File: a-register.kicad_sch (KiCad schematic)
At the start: 12 parts

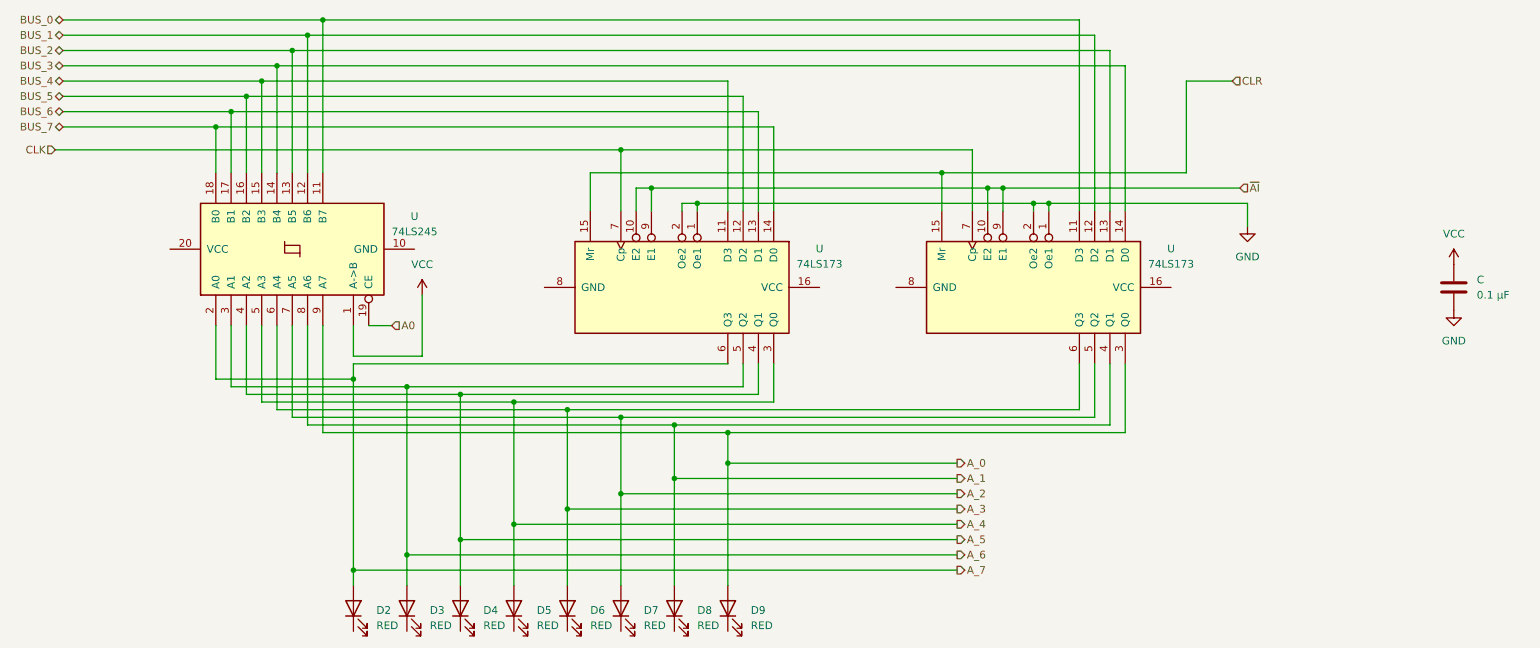
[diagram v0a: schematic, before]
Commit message: Added the ALU and flags register schematic.
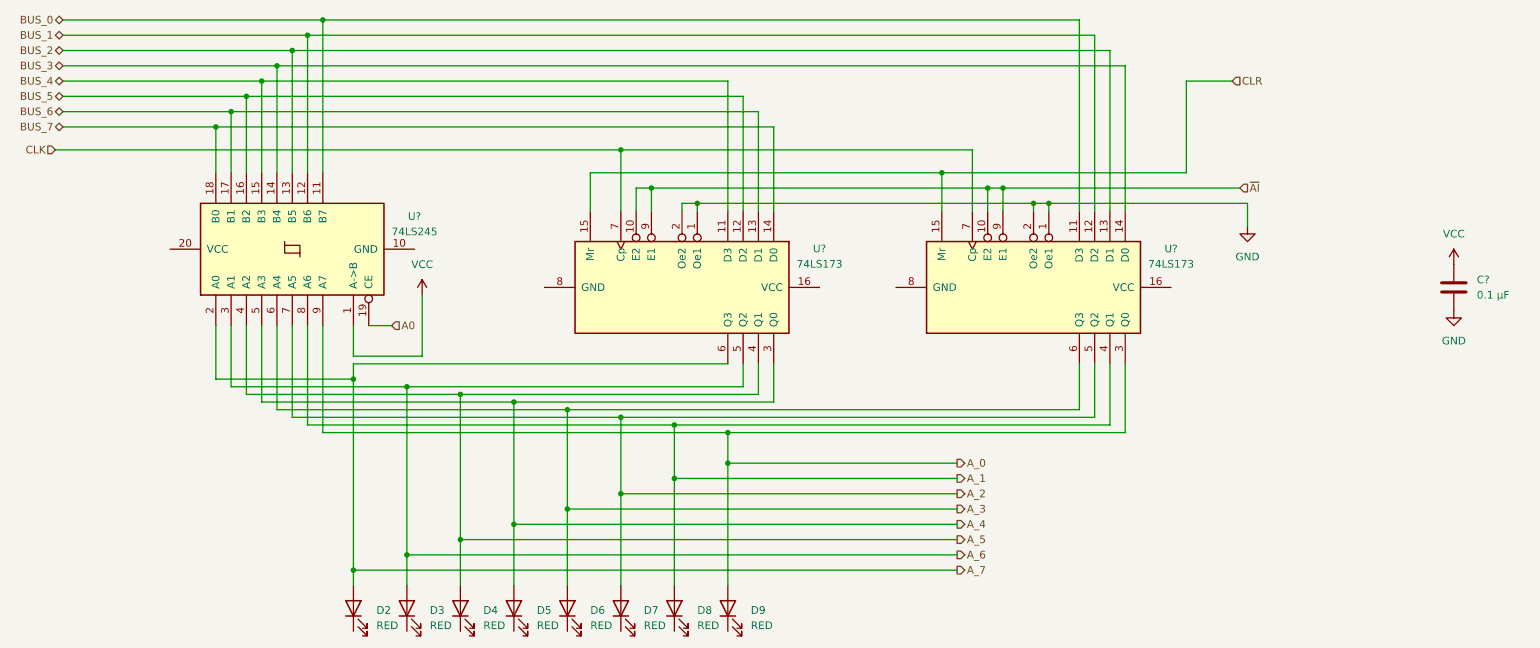
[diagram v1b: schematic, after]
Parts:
- renumbered C to C?, U to U?
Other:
- title: (none) -> 8 bit PC
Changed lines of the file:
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@@
 	(generator_version "9.0")
 	(paper "A4")
+	(title_block
+		(title "8 bit PC")
+		(date "2025-10-14")
+		(rev "1")
+	)
 	(junction
 		(at 57.15 35.56)
@@
 		(instances
 			(project "8-Bit-PC"
-				(path "/48633dea-2de9-4b6f-aeff-2ee54233f918/01639e59-f640-4704-bff8-92b5a7e3f002"
-					(reference "D16")
-					(unit 1)
-				)
 				(path "/48633dea-2de9-4b6f-aeff-2ee54233f918/0da64945-ad09-4cb6-87e6-9538c18b83c8"
 					(reference "D8")
@@
 		(instances
 			(project "8-Bit-PC"
-				(path "/48633dea-2de9-4b6f-aeff-2ee54233f918/01639e59-f640-4704-bff8-92b5a7e3f002"
-					(reference "D15")
-					(unit 1)
-				)
 				(path "/48633dea-2de9-4b6f-aeff-2ee54233f918/0da64945-ad09-4cb6-87e6-9538c18b83c8"
 					(reference "D7")
@@
 		(dnp no)
 		(fields_autoplaced yes)
-		(property "Reference" "U"
+		(property "Reference" "U?"
 			(at 213.36 58.3498 90)
 			(effects
@@
 		(instances
 			(project "8-Bit-PC"
-				(path "/48633dea-2de9-4b6f-aeff-2ee54233f918/01639e59-f640-4704-bff8-92b5a7e3f002"
-					(reference "U12")
+				(path "/48633dea-2de9-4b6f-aeff-2ee54233f918/0da64945-ad09-4cb6-87e6-9538c18b83c8"
+					(reference "U?")
 					(unit 1)
 				)
@@
 		(dnp no)
 		(fields_autoplaced yes)
-		(property "Reference" "#PWR"
+		(property "Reference" "#PWR?"
 			(at 260.35 74.93 0)
 			(effects
@@
 		(instances
 			(project "8-Bit-PC"
-				(path "/48633dea-2de9-4b6f-aeff-2ee54233f918/01639e59-f640-4704-bff8-92b5a7e3f002"
-					(reference "#PWR017")
+				(path "/48633dea-2de9-4b6f-aeff-2ee54233f918/0da64945-ad09-4cb6-87e6-9538c18b83c8"
+					(reference "#PWR?")
 					(unit 1)
 				)
@@
 		(dnp no)
 		(fields_autoplaced yes)
-		(property "Reference" "U"
+		(property "Reference" "U?"
 			(at 87.63 52.9746 90)
 			(effects
@@
 		(instances
 			(project "8-Bit-PC"
-				(path "/48633dea-2de9-4b6f-aeff-2ee54233f918/01639e59-f640-4704-bff8-92b5a7e3f002"
-					(reference "U10")
+				(path "/48633dea-2de9-4b6f-aeff-2ee54233f918/0da64945-ad09-4cb6-87e6-9538c18b83c8"
+					(reference "U?")
 					(unit 1)
 				)
@@
 		(dnp no)
 		(fields_autoplaced yes)
-		(property "Reference" "#PWR"
+		(property "Reference" "#PWR?"
 			(at 226.06 60.96 0)
 			(effects
@@
 		(instances
 			(project "8-Bit-PC"
-				(path "/48633dea-2de9-4b6f-aeff-2ee54233f918/01639e59-f640-4704-bff8-92b5a7e3f002"
-					(reference "#PWR015")
+				(path "/48633dea-2de9-4b6f-aeff-2ee54233f918/0da64945-ad09-4cb6-87e6-9538c18b83c8"
+					(reference "#PWR?")
 					(unit 1)
 				)
@@
 		(dnp no)
 		(fields_autoplaced yes)
-		(property "Reference" "#PWR"
+		(property "Reference" "#PWR?"
 			(at 260.35 64.77 0)
 			(effects
@@
 		(instances
 			(project "8-Bit-PC"
-				(path "/48633dea-2de9-4b6f-aeff-2ee54233f918/01639e59-f640-4704-bff8-92b5a7e3f002"
-					(reference "#PWR016")
+				(path "/48633dea-2de9-4b6f-aeff-2ee54233f918/0da64945-ad09-4cb6-87e6-9538c18b83c8"
+					(reference "#PWR?")
 					(unit 1)
 				)
@@
 		(instances
 			(project "8-Bit-PC"
-				(path "/48633dea-2de9-4b6f-aeff-2ee54233f918/01639e59-f640-4704-bff8-92b5a7e3f002"
-					(reference "D10")
-					(unit 1)
-				)
 				(path "/48633dea-2de9-4b6f-aeff-2ee54233f918/0da64945-ad09-4cb6-87e6-9538c18b83c8"
 					(reference "D2")
@@
 		(dnp no)
 		(fields_autoplaced yes)
-		(property "Reference" "C"
+		(property "Reference" "C?"
 			(at 264.16 63.4999 0)
 			(effects
@@
 		(instances
 			(project "8-Bit-PC"
-				(path "/48633dea-2de9-4b6f-aeff-2ee54233f918/01639e59-f640-4704-bff8-92b5a7e3f002"
-					(reference "C9")
+				(path "/48633dea-2de9-4b6f-aeff-2ee54233f918/0da64945-ad09-4cb6-87e6-9538c18b83c8"
+					(reference "C?")
 					(unit 1)
 				)
@@
 		(instances
 			(project "8-Bit-PC"
-				(path "/48633dea-2de9-4b6f-aeff-2ee54233f918/01639e59-f640-4704-bff8-92b5a7e3f002"
-					(reference "D11")
-					(unit 1)
-				)
 				(path "/48633dea-2de9-4b6f-aeff-2ee54233f918/0da64945-ad09-4cb6-87e6-9538c18b83c8"
 					(reference "D3")
@@
 		(dnp no)
 		(fields_autoplaced yes)
-		(property "Reference" "#PWR"
+		(property "Reference" "#PWR?"
 			(at 88.9 69.85 0)
 			(effects
@@
 		(instances
 			(project "8-Bit-PC"
-				(path "/48633dea-2de9-4b6f-aeff-2ee54233f918/01639e59-f640-4704-bff8-92b5a7e3f002"
-					(reference "#PWR014")
+				(path "/48633dea-2de9-4b6f-aeff-2ee54233f918/0da64945-ad09-4cb6-87e6-9538c18b83c8"
+					(reference "#PWR?")
 					(unit 1)
 				)
@@
 		(instances
 			(project "8-Bit-PC"
-				(path "/48633dea-2de9-4b6f-aeff-2ee54233f918/01639e59-f640-4704-bff8-92b5a7e3f002"
-					(reference "D12")
-					(unit 1)
-				)
 				(path "/48633dea-2de9-4b6f-aeff-2ee54233f918/0da64945-ad09-4cb6-87e6-9538c18b83c8"
 					(reference "D4")
@@
 		(dnp no)
 		(fields_autoplaced yes)
-		(property "Reference" "U"
+		(property "Reference" "U?"
 			(at 154.94 58.3498 90)
 			(effects
@@
 		(instances
 			(project "8-Bit-PC"
-				(path "/48633dea-2de9-4b6f-aeff-2ee54233f918/01639e59-f640-4704-bff8-92b5a7e3f002"
-					(reference "U11")
+				(path "/48633dea-2de9-4b6f-aeff-2ee54233f918/0da64945-ad09-4cb6-87e6-9538c18b83c8"
+					(reference "U?")
 					(unit 1)
 				)
@@
 		(instances
 			(project "8-Bit-PC"
-				(path "/48633dea-2de9-4b6f-aeff-2ee54233f918/01639e59-f640-4704-bff8-92b5a7e3f002"
-					(reference "D13")
-					(unit 1)
-				)
 				(path "/48633dea-2de9-4b6f-aeff-2ee54233f918/0da64945-ad09-4cb6-87e6-9538c18b83c8"
 					(reference "D5")
@@
 		(instances
 			(project "8-Bit-PC"
-				(path "/48633dea-2de9-4b6f-aeff-2ee54233f918/01639e59-f640-4704-bff8-92b5a7e3f002"
-					(reference "D17")
-					(unit 1)
-				)
 				(path "/48633dea-2de9-4b6f-aeff-2ee54233f918/0da64945-ad09-4cb6-87e6-9538c18b83c8"
 					(reference "D9")
@@
 		(instances
 			(project "8-Bit-PC"
-				(path "/48633dea-2de9-4b6f-aeff-2ee54233f918/01639e59-f640-4704-bff8-92b5a7e3f002"
-					(reference "D14")
-					(unit 1)
-				)
 				(path "/48633dea-2de9-4b6f-aeff-2ee54233f918/0da64945-ad09-4cb6-87e6-9538c18b83c8"
 					(reference "D6")
